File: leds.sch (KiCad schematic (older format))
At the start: 8 parts

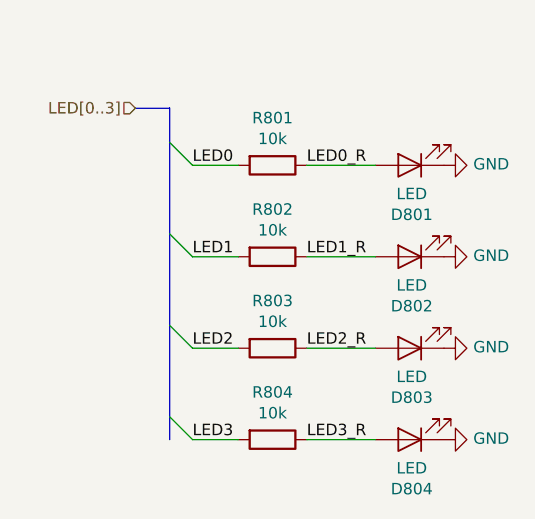
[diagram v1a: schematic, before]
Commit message: connect the non-fpga pin of the leds to vcc insted of gnd
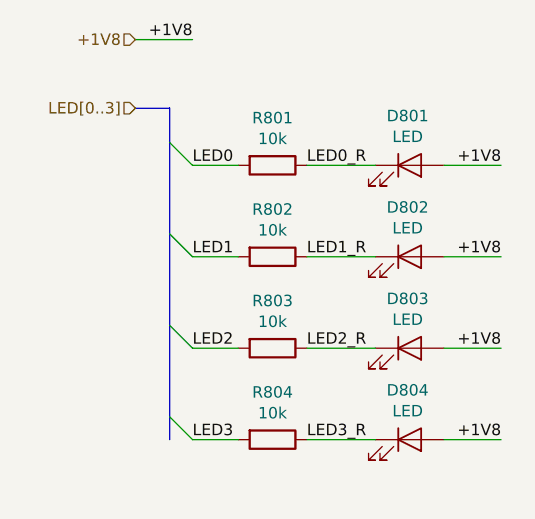
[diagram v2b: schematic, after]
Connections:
- net LED0_R: now also D801.1 (K); no longer D801.2 (A)
- net LED1_R: now also D802.1 (K); no longer D802.2 (A)
- net LED2_R: now also D803.1 (K); no longer D803.2 (A)
- net LED3_R: now also D804.1 (K); no longer D804.2 (A)
- removed net GND: D801.1 (K), D802.1 (K), D803.1 (K), D804.1 (K)
- new net +1V8: D801.2 (A), D802.2 (A), D803.2 (A), D804.2 (A)
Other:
- moved on the sheet: D801, D802, D803, D804
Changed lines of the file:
@@
 F 3 "~" H 4450 4600 50  0001 C CNN
 	1    4450 4600
-	-1   0    0    1
+	1    0    0    -1
 $EndComp
 $Comp
@@
 F 3 "~" H 4450 4200 50  0001 C CNN
 	1    4450 4200
-	-1   0    0    1
+	1    0    0    -1
 $EndComp
 $Comp
@@
 F 3 "~" H 4450 3800 50  0001 C CNN
 	1    4450 3800
-	-1   0    0    1
+	1    0    0    -1
 $EndComp
 $Comp
@@
 F 3 "~" H 4450 3400 50  0001 C CNN
 	1    4450 3400
-	-1   0    0    1
-$EndComp
-$Comp
-L power:GND #PWR0804
-U 1 1 5AFE2D24
-P 4600 4600
-F 0 "#PWR0804" H 4600 4350 50  0001 C CNN
-F 1 "GND" V 4605 4472 50  0000 R CNN
-F 2 "" H 4600 4600 50  0001 C CNN
-F 3 "" H 4600 4600 50  0001 C CNN
-	1    4600 4600
-	0    -1   -1   0
-$EndComp
-$Comp
-L power:GND #PWR0801
-U 1 1 5AFE2D74
-P 4600 3400
-F 0 "#PWR0801" H 4600 3150 50  0001 C CNN
-F 1 "GND" V 4605 3272 50  0000 R CNN
-F 2 "" H 4600 3400 50  0001 C CNN
-F 3 "" H 4600 3400 50  0001 C CNN
-	1    4600 3400
-	0    -1   -1   0
-$EndComp
-$Comp
-L power:GND #PWR0802
-U 1 1 5AFE2D87
-P 4600 3800
-F 0 "#PWR0802" H 4600 3550 50  0001 C CNN
-F 1 "GND" V 4605 3672 50  0000 R CNN
-F 2 "" H 4600 3800 50  0001 C CNN
-F 3 "" H 4600 3800 50  0001 C CNN
-	1    4600 3800
-	0    -1   -1   0
-$EndComp
-$Comp
-L power:GND #PWR0803
-U 1 1 5AFE2DC6
-P 4600 4200
-F 0 "#PWR0803" H 4600 3950 50  0001 C CNN
-F 1 "GND" V 4605 4072 50  0000 R CNN
-F 2 "" H 4600 4200 50  0001 C CNN
-F 3 "" H 4600 4200 50  0001 C CNN
-	1    4600 4200
-	0    -1   -1   0
+	1    0    0    -1
 $EndComp
 $Comp
@@
 Text Label 4000 4600 0    50   ~ 0
 LED3_R
+Text HLabel 3250 2850 0    50   Input ~ 0
++1V8
+Wire Wire Line
+	3500 2850 3250 2850
+Text Label 3500 2850 2    50   ~ 0
++1V8
+Wire Wire Line
+	4850 3400 4600 3400
+Text Label 4850 3400 2    50   ~ 0
++1V8
+Wire Wire Line
+	4850 3800 4600 3800
+Text Label 4850 3800 2    50   ~ 0
++1V8
+Wire Wire Line
+	4850 4200 4600 4200
+Text Label 4850 4200 2    50   ~ 0
++1V8
+Wire Wire Line
+	4850 4600 4600 4600
+Text Label 4850 4600 2    50   ~ 0
++1V8
 Wire Bus Line
 	3400 3150 3400 4600

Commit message: connect leds to 3v3 power supply rail
the led is still connected to a 1v8 fpga io bank though
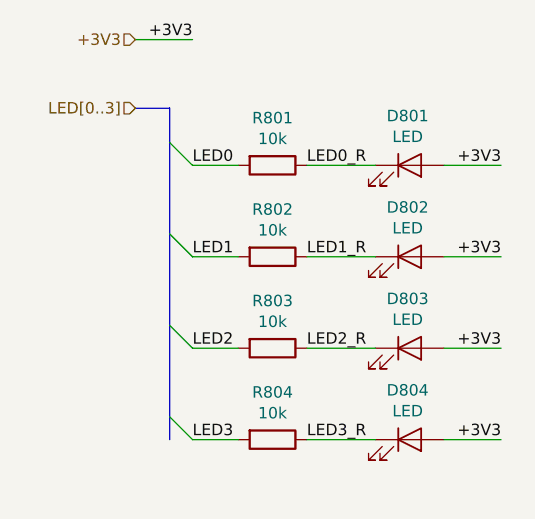
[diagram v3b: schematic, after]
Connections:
- net +1V8 renamed +3V3
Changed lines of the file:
@@
 LED3_R
 Text HLabel 3250 2850 0    50   Input ~ 0
-+1V8
++3V3
 Wire Wire Line
 	3500 2850 3250 2850
 Text Label 3500 2850 2    50   ~ 0
-+1V8
++3V3
 Wire Wire Line
 	4850 3400 4600 3400
 Text Label 4850 3400 2    50   ~ 0
-+1V8
++3V3
 Wire Wire Line
 	4850 3800 4600 3800
 Text Label 4850 3800 2    50   ~ 0
-+1V8
++3V3
 Wire Wire Line
 	4850 4200 4600 4200
 Text Label 4850 4200 2    50   ~ 0
-+1V8
++3V3
 Wire Wire Line
 	4850 4600 4600 4600
 Text Label 4850 4600 2    50   ~ 0
-+1V8
++3V3
 Wire Bus Line
 	3400 3150 3400 4600
